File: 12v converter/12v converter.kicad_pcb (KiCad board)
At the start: 2 copper layers, 65.7 x 46 mm, 23 parts, among them J1 Conn_01x02_Socket, J2 Conn_01x02_Socket, U1 LM2674N-3.3

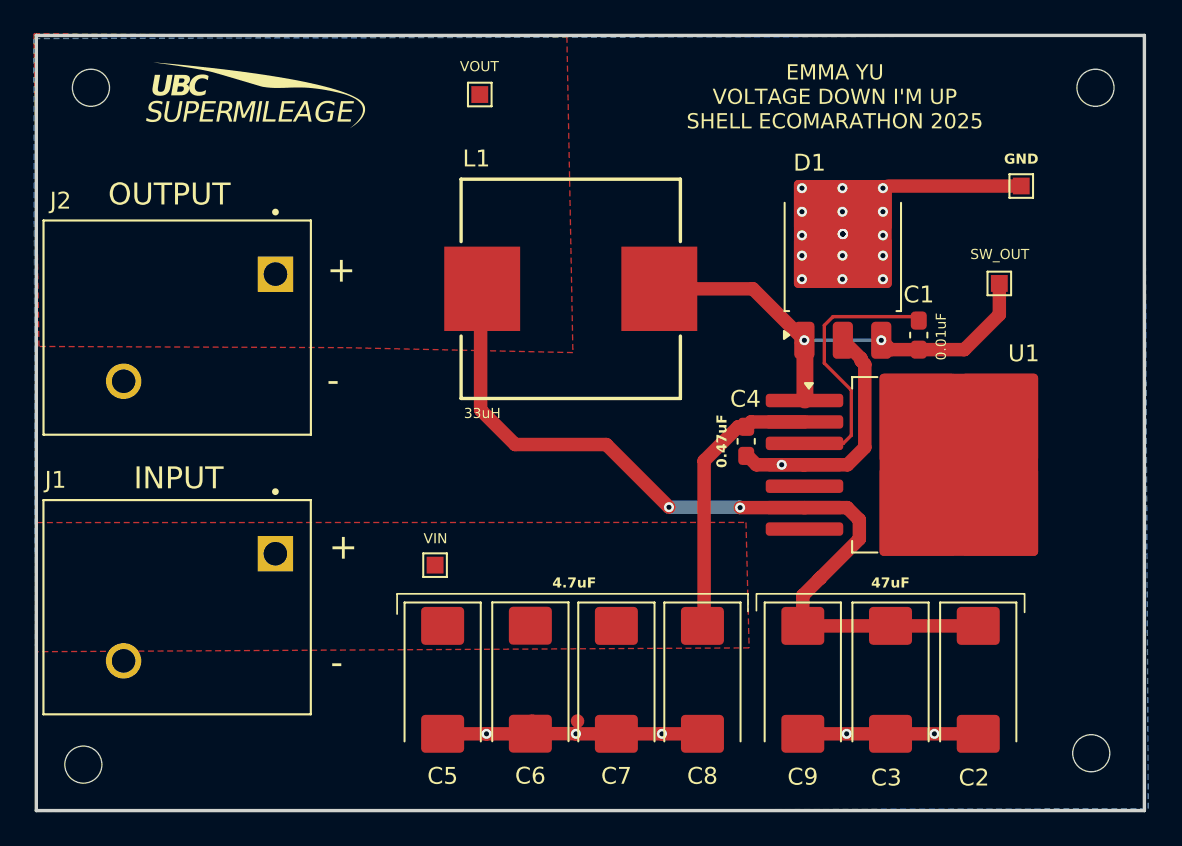
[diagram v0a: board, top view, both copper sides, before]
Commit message: pin reassignment, rerouting and changing position of SW_OUT and GND test points
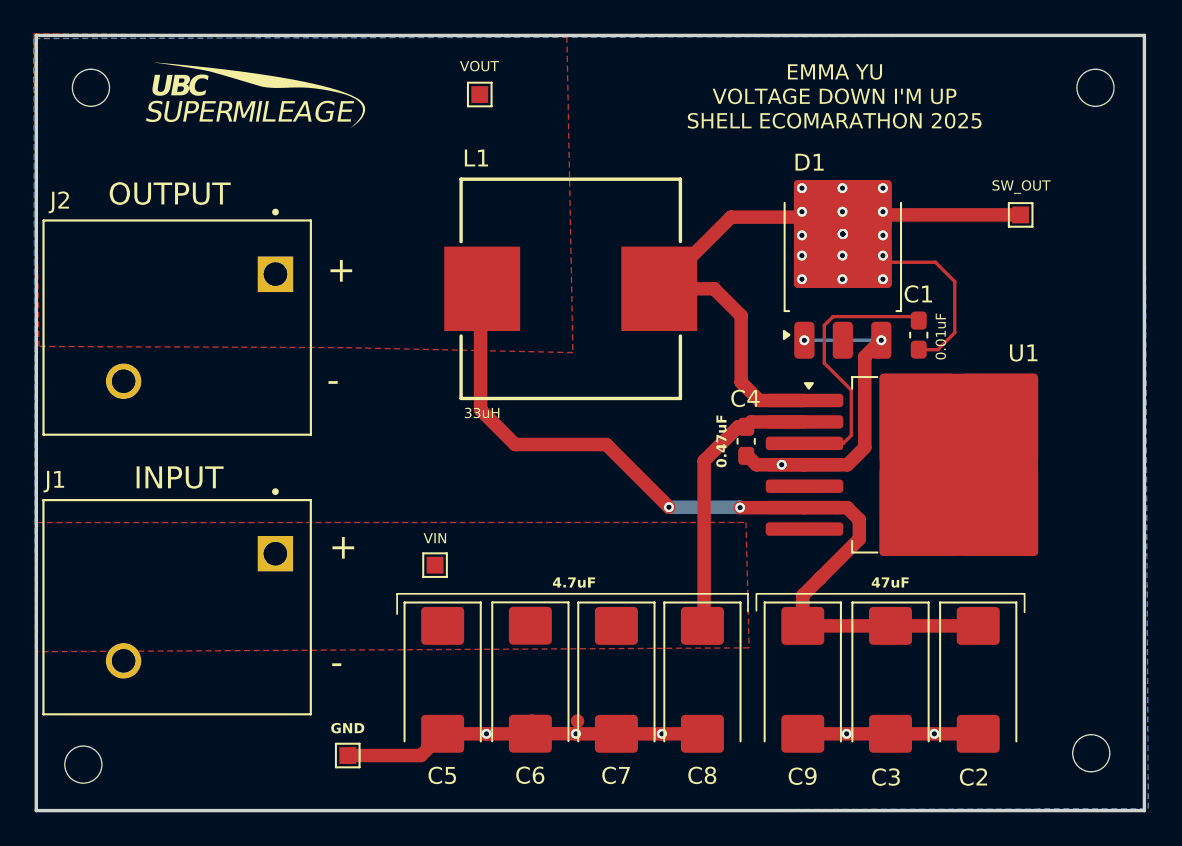
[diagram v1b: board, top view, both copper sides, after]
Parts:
- moved GND 52.3 mm to (137.1, 128.4)
- moved SW_OUT 4.26 mm to (177.0, 96.4)
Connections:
- D1 pad 1: /SW_OUT -> GND
- D1 pad 2: GND -> /SW_OUT
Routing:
- net /SW_OUT: track 28.2 -> 54.2 mm, vias 2 -> 17
- net GND: track 53.6 -> 51.3 mm, vias 23 -> 8

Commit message: changed D1 footprint from TO-252-3 to TO-252 then altered it (only on board) to make the outer pins GND and the pad SW_OUT
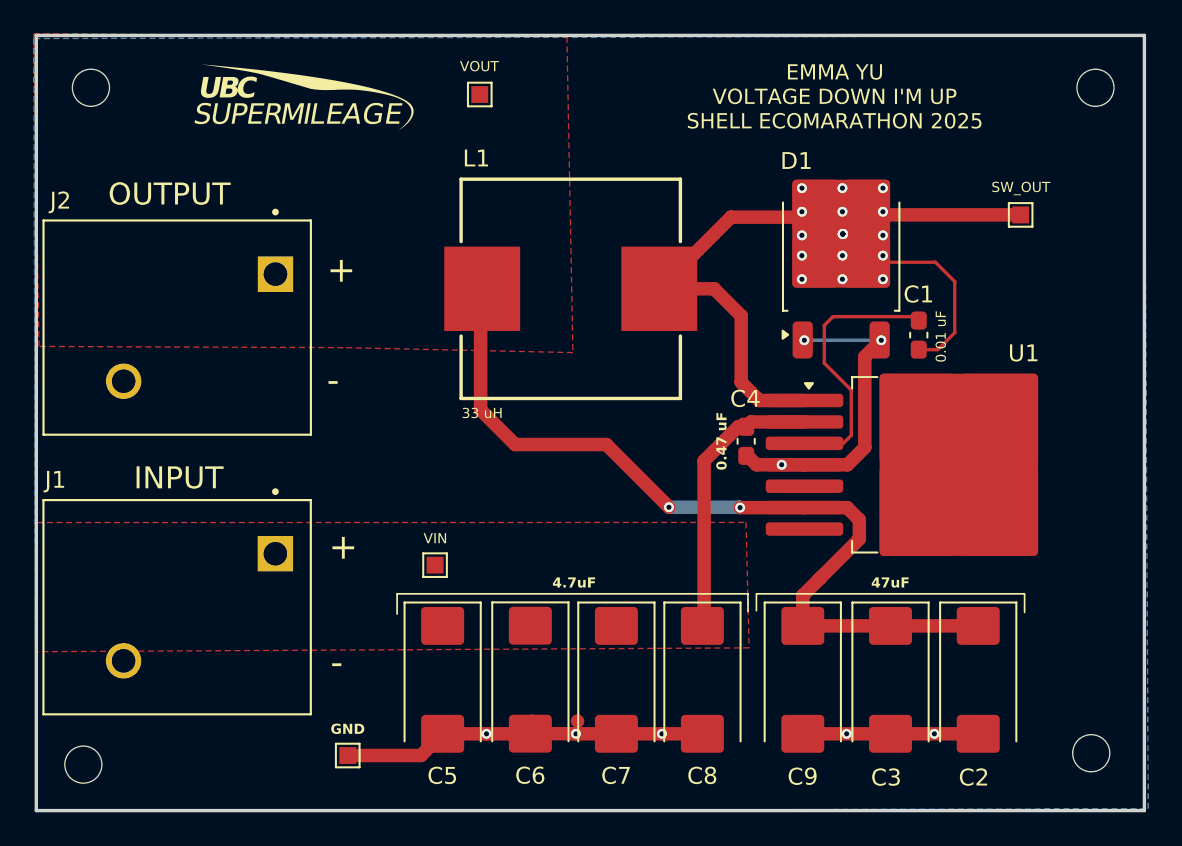
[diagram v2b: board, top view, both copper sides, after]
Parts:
- C1: value 0.01uF -> 0.01 uF
- C4: value 0.47uF -> 0.47 uF
- D1: footprint fcp12vconv_footprints:TO-252-3_TabPin2_Single -> Package_TO_SOT_SMD:TO-252-2
- L1: value 33uH -> 33 uH
- moved G*** 2.88 mm to (134.5, 89.4)
- moved D1 0.66 mm to (166.3, 98.8)
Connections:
- D1 pad 1: GND -> /SW_OUT
- D1 pad 2: /SW_OUT -> GND

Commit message: generated gerber and drill files
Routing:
- net /SW_OUT: track 54.2 -> 46.4 mm, vias 17 -> 0
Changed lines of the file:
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@@
+	)
+	(segment
+		(start 170.925 102.649998)
+		(end 170.400002 102.125)
+		(width 0.2)
+		(layer "F.Cu")
+		(net 1)
 	)
 	(segment
@@
 	)
 	(segment
+		(start 166.925 106.775)
+		(end 166.925 109.455001)
+		(width 0.2)
+		(layer "F.Cu")
+		(net 1)
+	)
+	(segment
 		(start 165.325 102.932036)
 		(end 165.325 105.175)
@@
 	)
 	(segment
-		(start 165.838477 102.418559)
+		(start 166.132036 102.125)
 		(end 165.325 102.932036)
 		(width 0.2)
@@
 	)
 	(segment
-		(start 170.925 102.649998)
-		(end 170.693561 102.418559)
-		(width 0.2)
-		(layer "F.Cu")
-		(net 1)
-	)
-	(segment
-		(start 166.925 106.775)
-		(end 166.925 109.455001)
-		(width 0.2)
-		(layer "F.Cu")
-		(net 1)
-	)
-	(segment
-		(start 170.693561 102.418559)
-		(end 165.838477 102.418559)
+		(start 170.400002 102.125)
+		(end 166.132036 102.125)
 		(width 0.2)
 		(layer "F.Cu")
@@
 	)
 	(segment
-		(start 150.691314 126.391314)
-		(end 150.7 126.4)
-		(width 0.8)
-		(layer "F.Cu")
-		(net 3)
-	)
-	(segment
 		(start 155.7 127.15)
 		(end 158.1 127.15)
@@
 	)
 	(segment
-		(start 176.96492 96.387346)
-		(end 167.554434 96.387346)
-		(width 0.8)
-		(layer "F.Cu")
-		(net 12)
-	)
-	(segment
-		(start 171.91436 99.193559)
-		(end 167.948221 99.193559)
-		(width 0.2)
-		(layer "F.Cu")
-		(net 12)
-	)
-	(segment
-		(start 173.059743 103.368073)
-		(end 173.059743 100.338942)
+		(start 173.059743 100.338942)
+		(end 173.059743 103.368073)
+		(width 0.2)
+		(layer "F.Cu")
+		(net 12)
+	)
+	(segment
+		(start 167.868559 99.193559)
+		(end 171.91436 99.193559)
+		(width 0.2)
+		(layer "F.Cu")
+		(net 12)
+	)
+	(segment
+		(start 164.8 95.825)
+		(end 164.729662 95.825)
+		(width 0.2)
+		(layer "F.Cu")
+		(net 12)
+	)
+	(segment
+		(start 172.052816 104.375)
+		(end 170.925 104.375)
+		(width 0.2)
+		(layer "F.Cu")
+		(net 12)
+	)
+	(segment
+		(start 167.437654 96.387346)
+		(end 176.96492 96.387346)
+		(width 0.8)
+		(layer "F.Cu")
+		(net 12)
+	)
+	(segment
+		(start 164.8 95.825)
+		(end 164.8 95.895338)
 		(width 0.2)
 		(layer "F.Cu")
@@
 	)
 	(segment
-		(start 173.059743 100.338942)
-		(end 171.91436 99.193559)
-		(width 0.2)
-		(layer "F.Cu")
-		(net 12)
-	)
-	(segment
 		(start 158.798744 100.769343)
 		(end 155.543804 100.769343)
@@
 	)
 	(segment
-		(start 165.424662 96.52)
-		(end 166.423221 97.518559)
-		(width 0.8)
-		(layer "F.Cu")
-		(net 12)
-	)
-	(segment
 		(start 164.15 107.39)
 		(end 161.474363 107.39)
@@
 	)
 	(segment
-		(start 163.829662 94.925)
-		(end 166.423221 97.518559)
-		(width 0.2)
-		(layer "F.Cu")
-		(net 12)
-	)
-	(segment
 		(start 159.793147 96.52)
 		(end 165.424662 96.52)
@@
 	)
 	(segment
-		(start 167.554434 96.387346)
-		(end 166.423221 97.518559)
-		(width 0.8)
+		(start 167.85 99.175)
+		(end 167.868559 99.193559)
+		(width 0.2)
+		(layer "F.Cu")
+		(net 12)
+	)
+	(segment
+		(start 173.059743 103.368073)
+		(end 172.052816 104.375)
+		(width 0.2)
 		(layer "F.Cu")
 		(net 12)
@@
 	)
 	(segment
-		(start 169.11678 94.675)
-		(end 167.948221 95.843559)
-		(width 0.2)
-		(layer "F.Cu")
-		(net 12)
-	)
-	(segment
-		(start 172.052816 104.375)
-		(end 173.059743 103.368073)
+		(start 167.96678 95.825)
+		(end 167.85 95.825)
+		(width 0.2)
+		(layer "F.Cu")
+		(net 12)
+	)
+	(segment
+		(start 171.91436 99.193559)
+		(end 173.059743 100.338942)
 		(width 0.2)
 		(layer "F.Cu")
@@
 		(net 12)
 	)
-	(segment
-		(start 170.925 104.375)
-		(end 172.052816 104.375)
-		(width 0.2)
-		(layer "F.Cu")
-		(net 12)
-	)
-	(via
-		(at 164 98.8)
-		(size 0.6)
-		(drill 0.3)
-		(layers "F.Cu" "B.Cu")
-		(net 12)
-	)
-	(via
-		(at 168.8 100.2)
-		(size 0.6)
-		(drill 0.3)
-		(layers "F.Cu" "B.Cu")
-		(net 12)
-	)
-	(via
-		(at 164 94.8)
-		(size 0.6)
-		(drill 0.3)
-		(layers "F.Cu" "B.Cu")
-		(net 12)
-	)
-	(via
-		(at 166.423221 97.518559)
-		(size 0.6)
-		(drill 0.3)
-		(layers "F.Cu" "B.Cu")
-		(net 12)
-	)
-	(via
-		(at 166.4 94.8)
-		(size 0.6)
-		(drill 0.3)
-		(layers "F.Cu" "B.Cu")
-		(net 12)
-	)
-	(via
-		(at 168.8 98.8)
-		(size 0.6)
-		(drill 0.3)
-		(layers "F.Cu" "B.Cu")
-		(net 12)
-	)
-	(via
-		(at 164 96.2)
-		(size 0.6)
-		(drill 0.3)
-		(layers "F.Cu" "B.Cu")
-		(net 12)
-	)
-	(via
-		(at 166.4 96.2)
-		(size 0.6)
-		(drill 0.3)
-		(layers "F.Cu" "B.Cu")
-		(net 12)
-	)
-	(via
-		(at 166.423221 97.518559)
-		(size 0.6)
-		(drill 0.3)
-		(layers "F.Cu" "B.Cu")
-		(net 12)
-	)
-	(via
-		(at 168.8 97.6)
-		(size 0.6)
-		(drill 0.3)
-		(layers "F.Cu" "B.Cu")
-		(net 12)
-	)
-	(via
-		(at 166.423221 97.518559)
-		(size 0.6)
-		(drill 0.3)
-		(layers "F.Cu" "B.Cu")
-		(net 12)
-	)
-	(via
-		(at 164 100.2)
-		(size 0.6)
-		(drill 0.3)
-		(layers "F.Cu" "B.Cu")
-		(net 12)
-	)
-	(via
-		(at 164 97.6)
-		(size 0.6)
-		(drill 0.3)
-		(layers "F.Cu" "B.Cu")
-		(net 12)
-	)
-	(via
-		(at 168.8 96.2)
-		(size 0.6)
-		(drill 0.3)
-		(layers "F.Cu" "B.Cu")
-		(net 12)
-	)
-	(via
-		(at 166.4 100.2)
-		(size 0.6)
-		(drill 0.3)
-		(layers "F.Cu" "B.Cu")
-		(net 12)
-	)
-	(via
-		(at 166.4 98.8)
-		(size 0.6)
-		(drill 0.3)
-		(layers "F.Cu" "B.Cu")
-		(net 12)
-	)
-	(via
-		(at 168.8 94.8)
-		(size 0.6)
-		(drill 0.3)
-		(layers "F.Cu" "B.Cu")
-		(net 12)
-	)
